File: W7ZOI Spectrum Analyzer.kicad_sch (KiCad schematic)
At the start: 0 parts

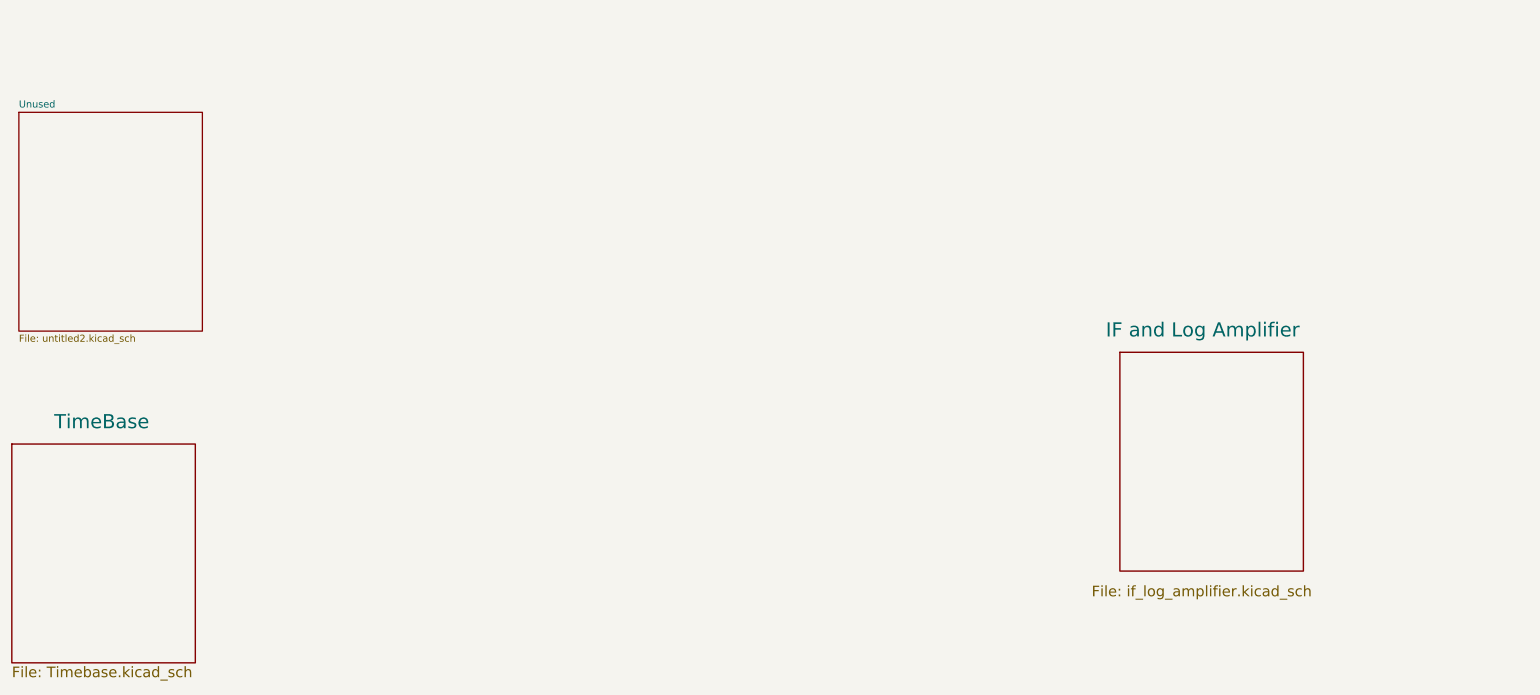
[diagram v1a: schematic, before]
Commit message: Resolution filters ltspice and kicad files
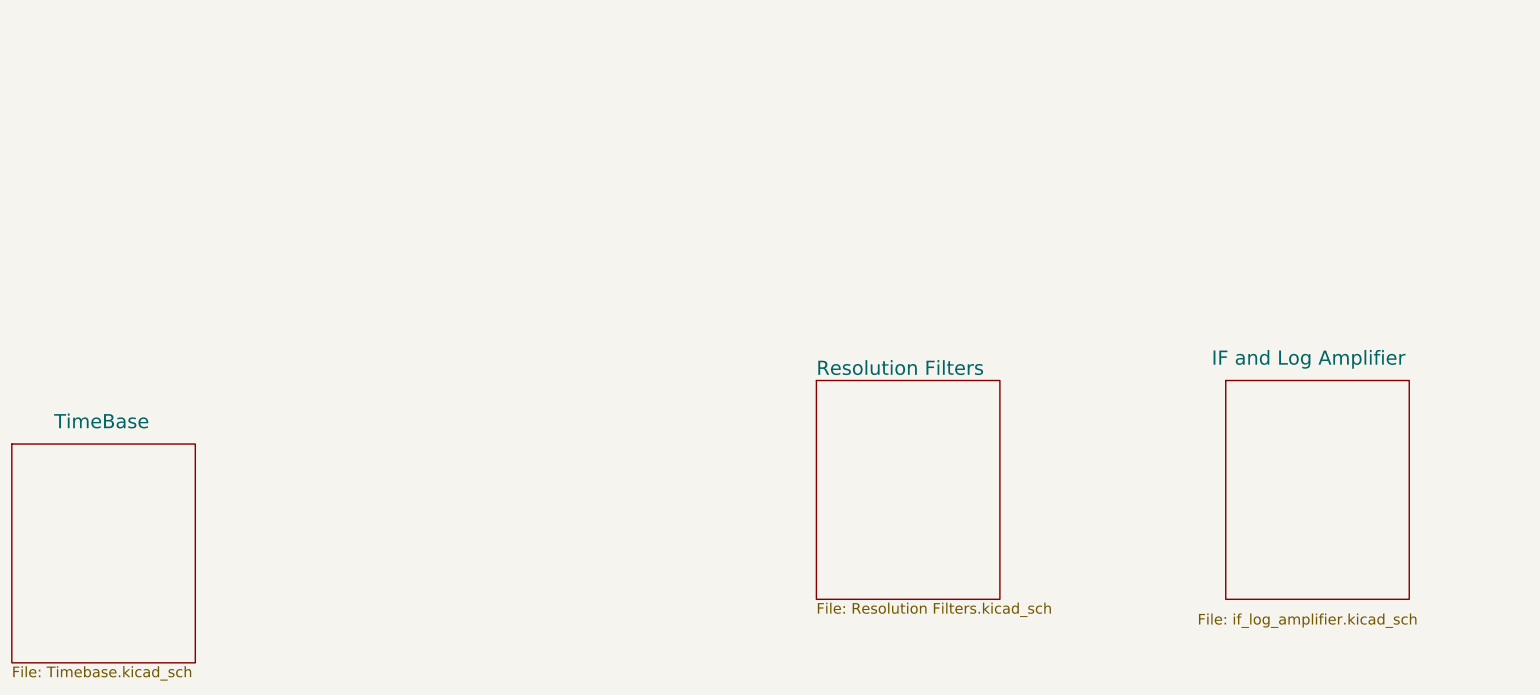
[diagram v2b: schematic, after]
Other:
- sheet Unused renamed Resolution Filters
- sheet Resolution Filters: file untitled2.kicad_sch -> Resolution Filters.kicad_sch

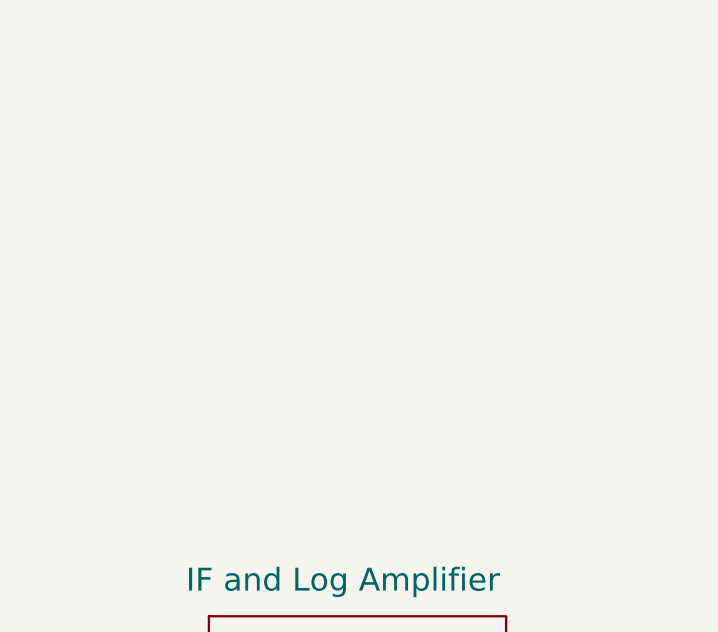
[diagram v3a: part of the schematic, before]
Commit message: Significant changes to timebase spice, 15v supply and resolution-filters
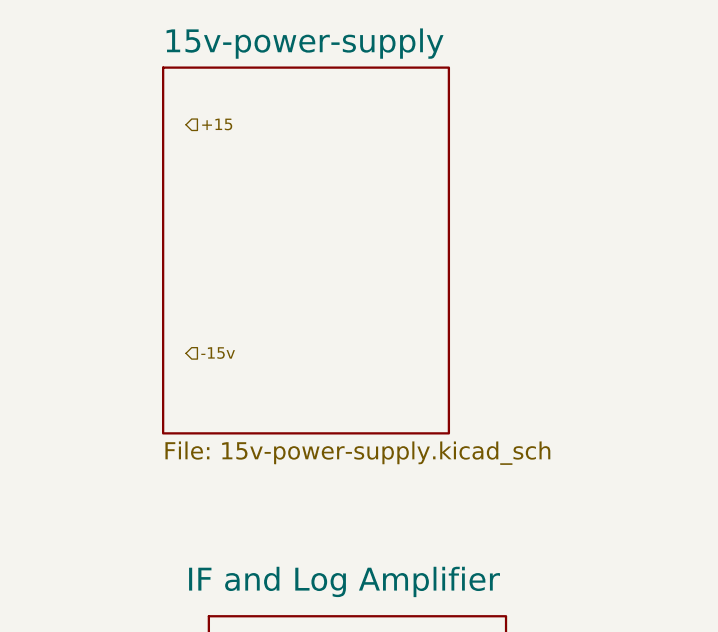
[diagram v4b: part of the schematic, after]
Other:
- added sheet 15v-power-supply (15v-power-supply.kicad_sch)
